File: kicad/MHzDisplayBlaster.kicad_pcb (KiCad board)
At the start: 2 copper layers, 50 x 39 mm, 7 parts, among them J1 Conn_02x15 DigitLHS, J2 Conn_02x15 DigitRHS, J3 Conn_01x03_Pin, U1 DC56-11GWA, U2 74LS04

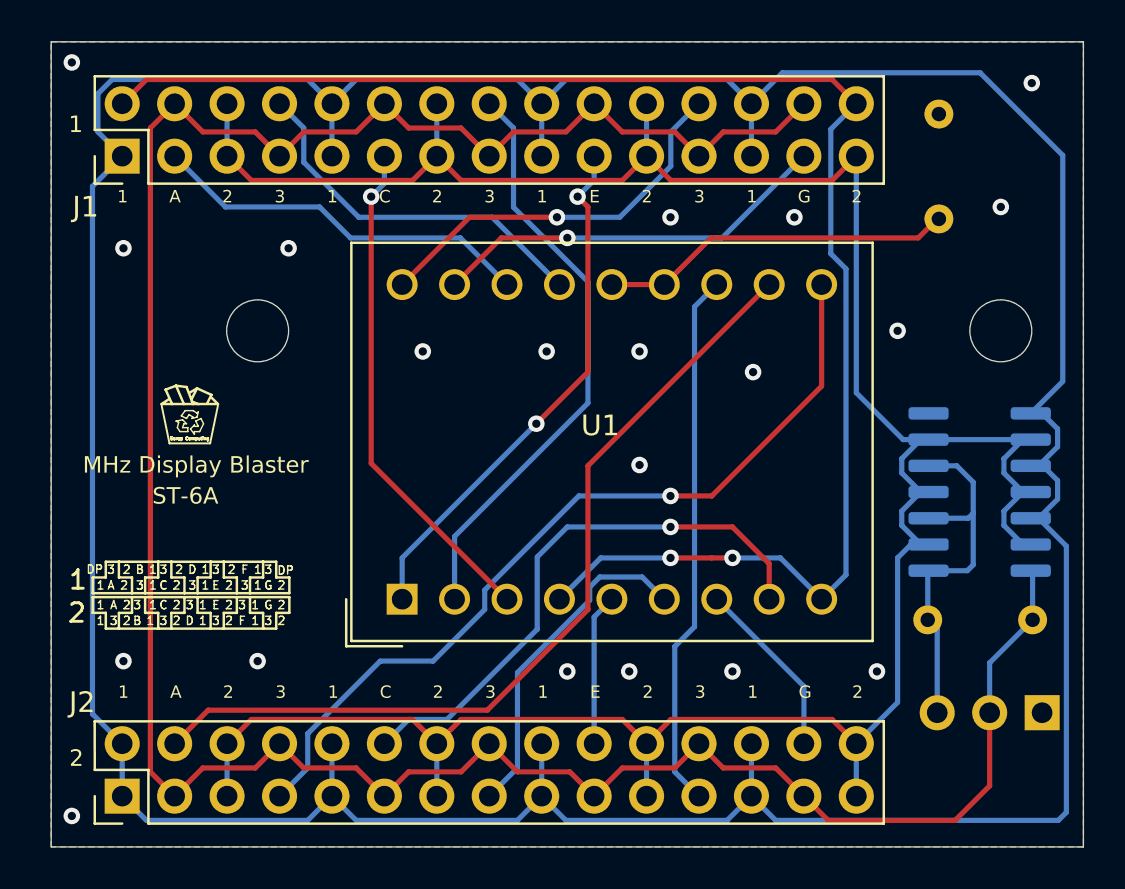
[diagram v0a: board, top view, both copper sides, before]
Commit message: Add Turbo LED Header
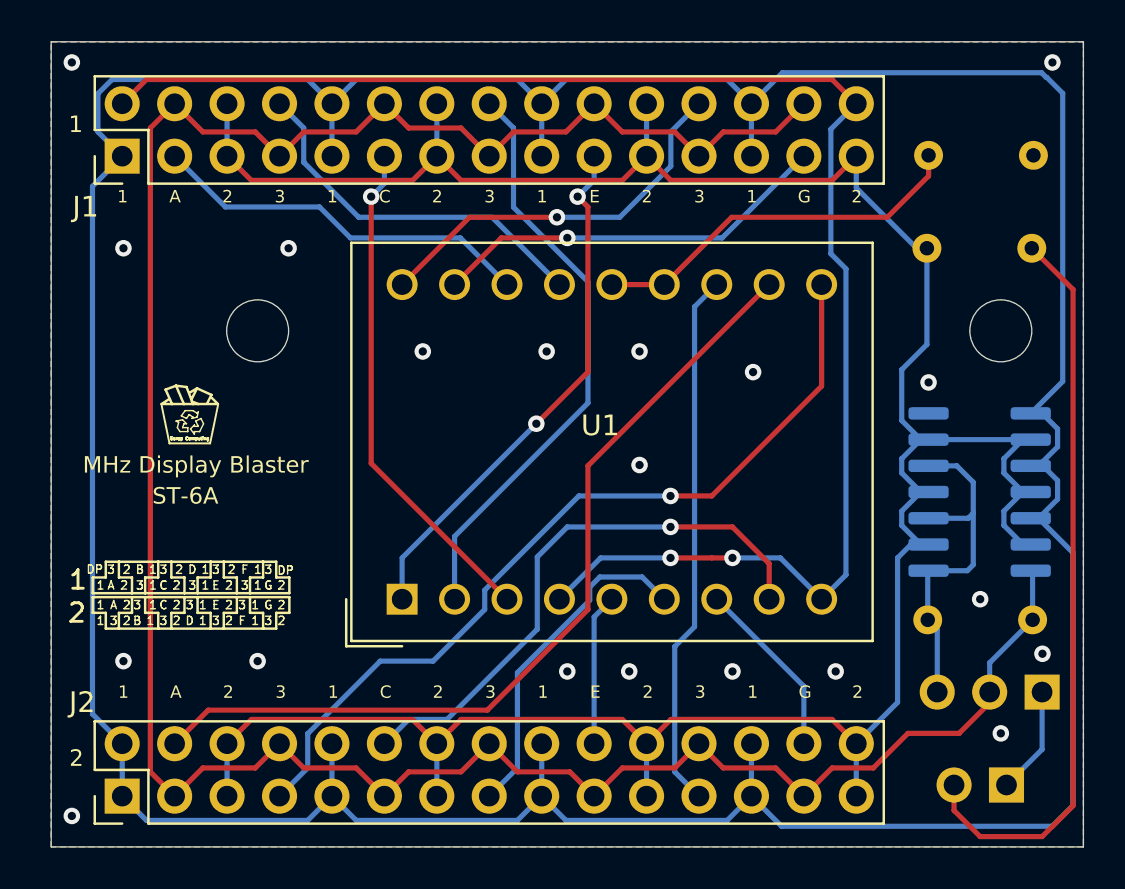
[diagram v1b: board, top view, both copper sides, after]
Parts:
- added J4: Conn_01x02_Pin, Connector_PinHeader_2.54mm:PinHeader_1x02_P2.54mm_Vertical, B.Cu at (146.3, 76.0)
- added R3: 1K, Resistor_THT:R_Axial_DIN0204_L3.6mm_D1.6mm_P5.08mm_Horizontal, B.Cu at (147.5, 50.0)
- moved R1 5.00 mm to (147.6, 45.5), turned to 180 degrees
- moved J3 1.00 mm to (148.0, 71.5)
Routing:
- net Net-(J4-Pin_2): track 0.00 -> 36.0 mm
- net GND: track 0.00 -> 5.71 mm
- net 3: track 129.6 -> 126.3 mm
- net 1: track 188.3 -> 190.5 mm
- net DIG1_CC: track 17.3 -> 18.5 mm
- net Turbo: track 18.1 -> 17.1 mm
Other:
- board text removed: "+5"
- board text removed: "Gnd"
- board text removed: "Trbo"

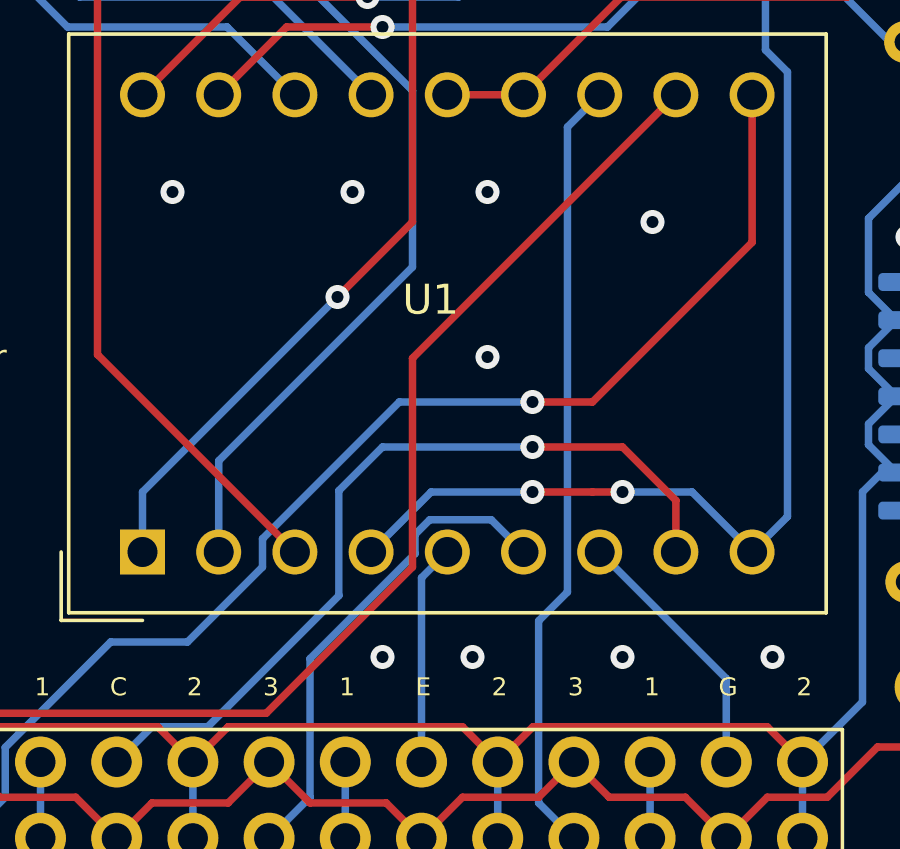
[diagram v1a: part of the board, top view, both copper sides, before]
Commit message: Adjust ground plane vias
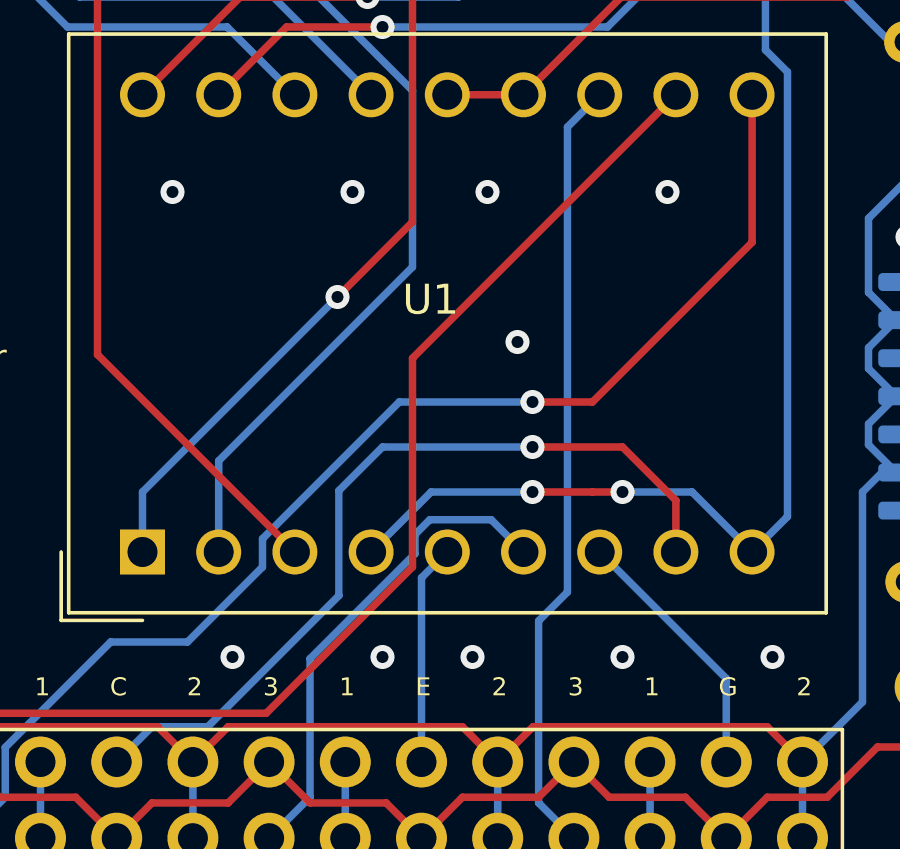
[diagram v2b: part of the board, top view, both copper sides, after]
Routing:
- net GND: vias 20 -> 21
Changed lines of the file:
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@@
   (via (at 133 70.5) (size 0.8) (drill 0.4) (layers "F.Cu" "B.Cu") (free) (net 21))
   (via (at 142.5 56.5) (size 0.8) (drill 0.4) (layers "F.Cu" "B.Cu") (free) (net 21))
-  (via (at 128.5 60.5) (size 0.8) (drill 0.4) (layers "F.Cu" "B.Cu") (free) (net 21))
+  (via (at 129.5 60) (size 0.8) (drill 0.4) (layers "F.Cu" "B.Cu") (free) (net 21))
   (via (at 103.5 70) (size 0.8) (drill 0.4) (layers "F.Cu" "B.Cu") (free) (net 21))
   (via (at 148.016689 69.644067) (size 0.8) (drill 0.4) (layers "F.Cu" "B.Cu") (free) (net 21))
@@
   (via (at 101 41) (size 0.8) (drill 0.4) (layers "F.Cu" "B.Cu") (free) (net 21))
   (via (at 110 70) (size 0.8) (drill 0.4) (layers "F.Cu" "B.Cu") (free) (net 21))
-  (via (at 134 56) (size 0.8) (drill 0.4) (layers "F.Cu" "B.Cu") (free) (net 21))
+  (via (at 134.5 55) (size 0.8) (drill 0.4) (layers "F.Cu" "B.Cu") (free) (net 21))
   (via (at 138 70.5) (size 0.8) (drill 0.4) (layers "F.Cu" "B.Cu") (free) (net 21))
   (via (at 125 70.5) (size 0.8) (drill 0.4) (layers "F.Cu" "B.Cu") (free) (net 21))
@@
   (via (at 128.5 55) (size 0.8) (drill 0.4) (layers "F.Cu" "B.Cu") (free) (net 21))
   (via (at 124 55) (size 0.8) (drill 0.4) (layers "F.Cu" "B.Cu") (free) (net 21))
+  (via (at 120 70.5) (size 0.8) (drill 0.4) (layers "F.Cu" "B.Cu") (free) (net 21))
   (via (at 148.5 41) (size 0.8) (drill 0.4) (layers "F.Cu" "B.Cu") (free) (net 21))
   (via (at 111.5 50) (size 0.8) (drill 0.4) (layers "F.Cu" "B.Cu") (free) (net 21))

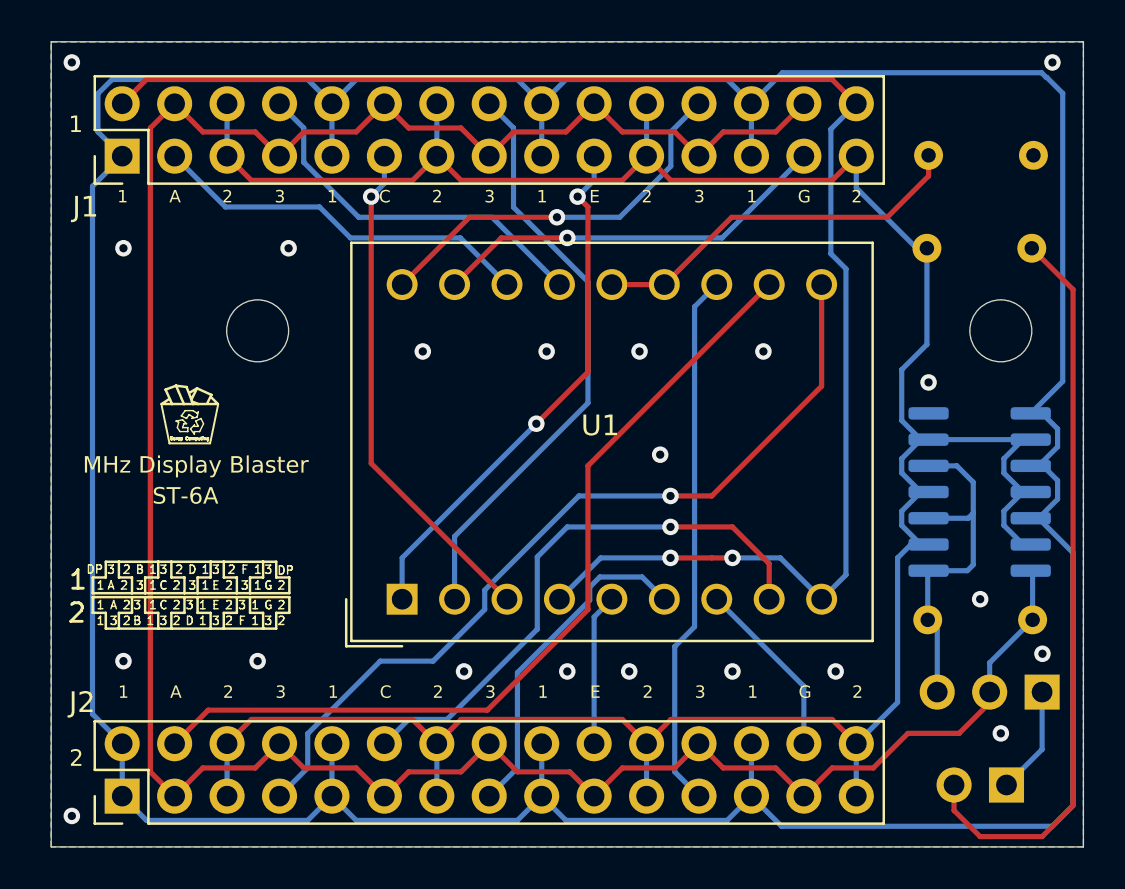
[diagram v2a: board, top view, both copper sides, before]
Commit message: Slight adjustment to display and mounting holes
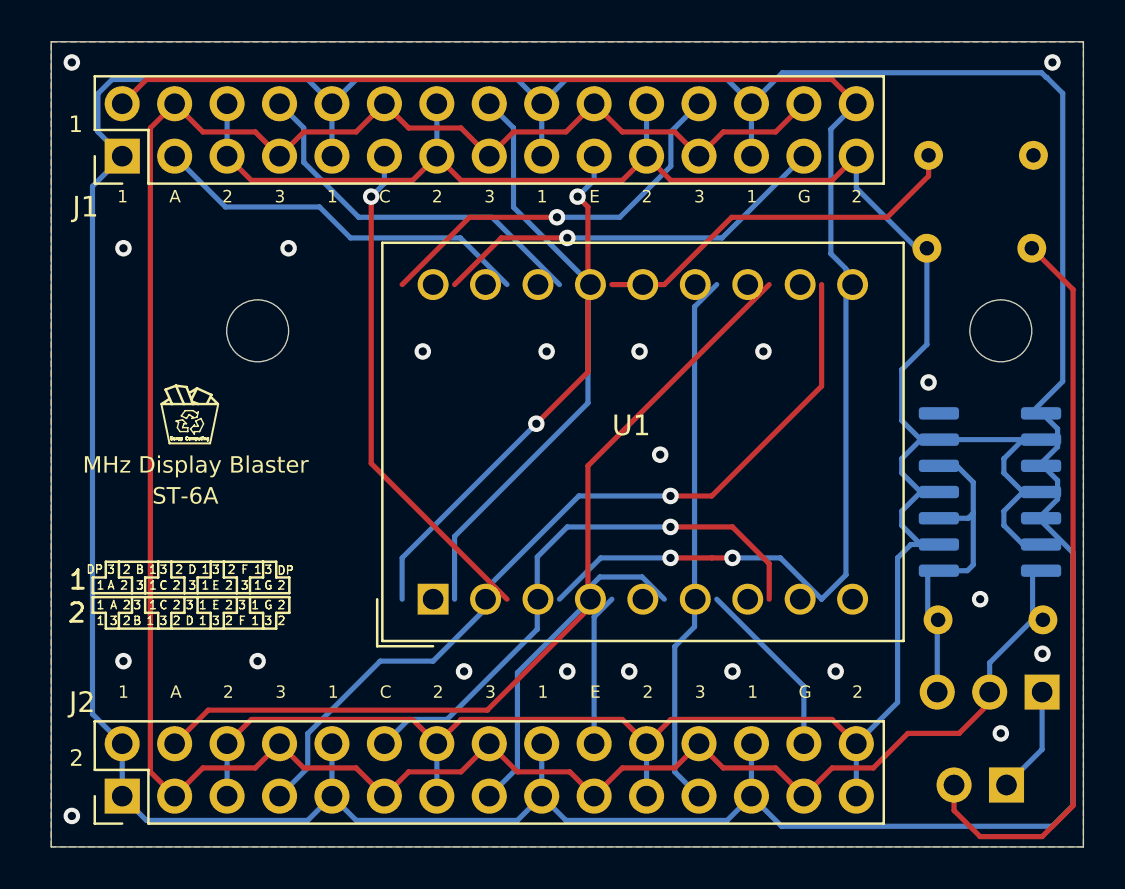
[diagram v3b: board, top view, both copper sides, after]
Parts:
- moved U1 1.50 mm to (118.5, 67.0)
- moved R2 0.50 mm to (148.0, 68.0)
- moved U2 0.50 mm to (145.5, 61.8)
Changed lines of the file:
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@@
   )
   (footprint "Display_7Segment:DA56-11CGKWA" locked (layer "F.Cu")
-    (at 117 67 90)
+    (at 118.5 67 90)
     (descr "http://www.kingbright.com/attachments/file/psearch/000/00/00/DA56-11CGKWA(Ver.16A).pdf")
     (tags "Double digit seven segment green LED display")
@@
   )
   (footprint "Resistor_THT:R_Axial_DIN0204_L3.6mm_D1.6mm_P5.08mm_Horizontal" (layer "B.Cu")
-    (at 147.54 68 180)
+    (at 148.04 68 180)
     (descr "Resistor, Axial_DIN0204 series, Axial, Horizontal, pin pitch=5.08mm, 0.167W, length*diameter=3.6*1.6mm^2, http://cdn-reichelt.de/documents/datenblatt/B400/1_4W%23YAG.pdf")
     (tags "Resistor Axial_DIN0204 series Axial Horizontal pin pitch 5.08mm 0.167W length 3.6mm diameter 1.6mm")
@@
   )
   (footprint "Package_SO:SOIC-14_3.9x8.7mm_P1.27mm" (layer "B.Cu")
-    (at 144.975 61.81)
+    (at 145.475 61.81)
     (descr "SOIC, 14 Pin (JEDEC MS-012AB, https://www.analog.com/media/en/package-pcb-resources/package/pkg_pdf/soic_narrow-r/r_14.pdf), generated with kicad-footprint-generator ipc_gullwing_generator.py")
     (tags "SOIC SO")

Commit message: Change HEX Inverter position, clean up layout
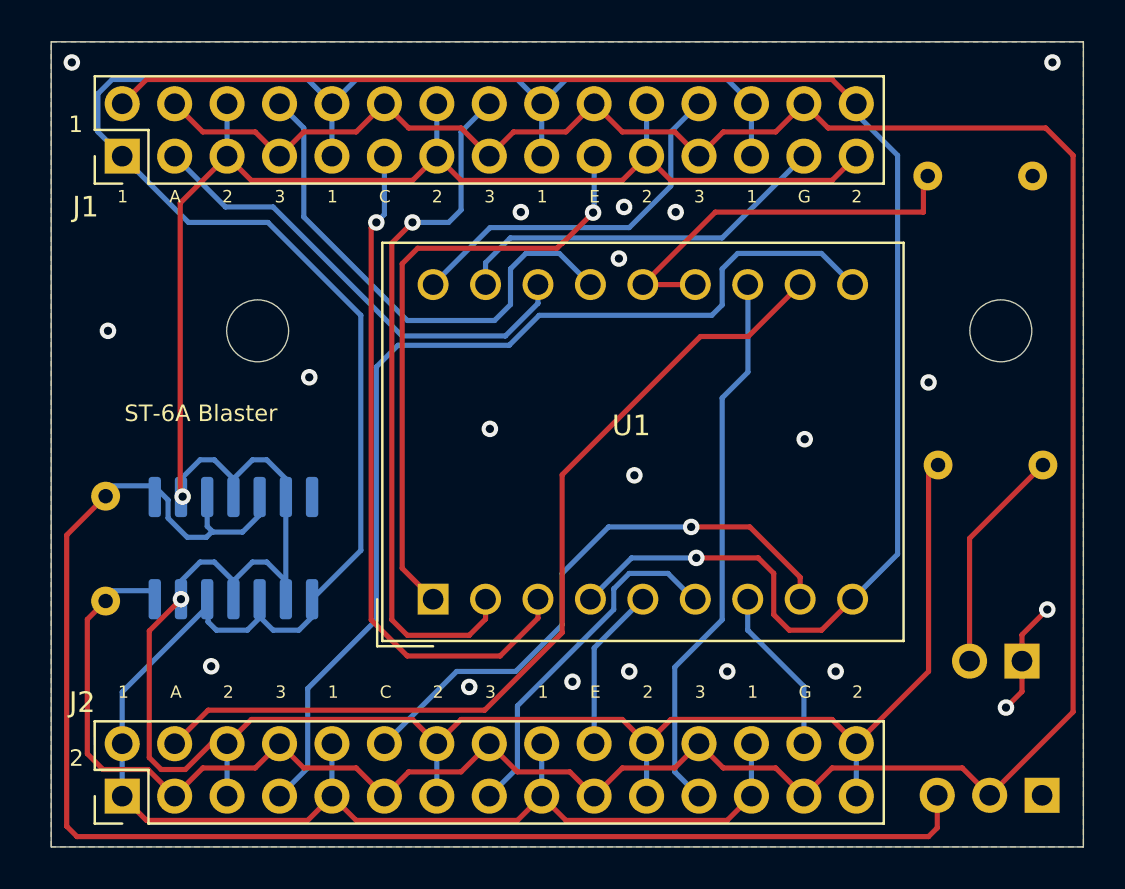
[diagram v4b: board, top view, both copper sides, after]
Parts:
- R3: value 1K -> 330
- moved R2 45.4 mm to (102.6, 67.1), turned to 90 degrees
- moved U2 36.7 mm to (108.8, 64.5), turned to -90 degrees
- moved R3 10.5 mm to (148.0, 60.5)
- moved J4 6.05 mm to (147.0, 70.0)
- moved J3 5.00 mm to (148.0, 76.5)
- moved R1 1.00 mm to (147.5, 46.5)
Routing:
- net Turbo: track 17.1 -> 74.6 mm
- net 1: track 190.5 -> 137.4 mm
- net Net-(J4-Pin_2): track 36.0 -> 11.0 mm
- net 3: track 126.3 -> 145.6 mm
- net 2: track 132.9 -> 150.1 mm, vias 0 -> 2
- net DIG2_B: track 40.9 -> 49.7 mm, vias 1 -> 0
- net DIG1_C: track 24.5 -> 33.2 mm
- net DIG1_B: track 18.2 -> 24.9 mm
- net DIG1_D: track 28.7 -> 34.1 mm, vias 0 -> 1
- net DIG1_E: track 25.7 -> 29.9 mm, vias 2 -> 1
- net DIG1_A: track 18.7 -> 22.8 mm
- net DP: track 76.2 -> 79.0 mm, vias 2 -> 1
- net DIG2_A: track 42.1 -> 44.0 mm
- net DIG1_F: track 19.0 -> 18.0 mm, vias 1 -> 0
- net DIG2_D: track 16.4 -> 17.3 mm
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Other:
- board text added: "330"
- board text added: "5v"
- board text added: "Gnd"
- board text added: "LED+"
- board text added: "LED-"
- board text added: "ST-6A Blaster"
- board text added: "Trbo"
- board text removed: "MHz Display Blaster"
- board text removed: "ST-6A"

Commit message: Rotate HEX inverter, finalize
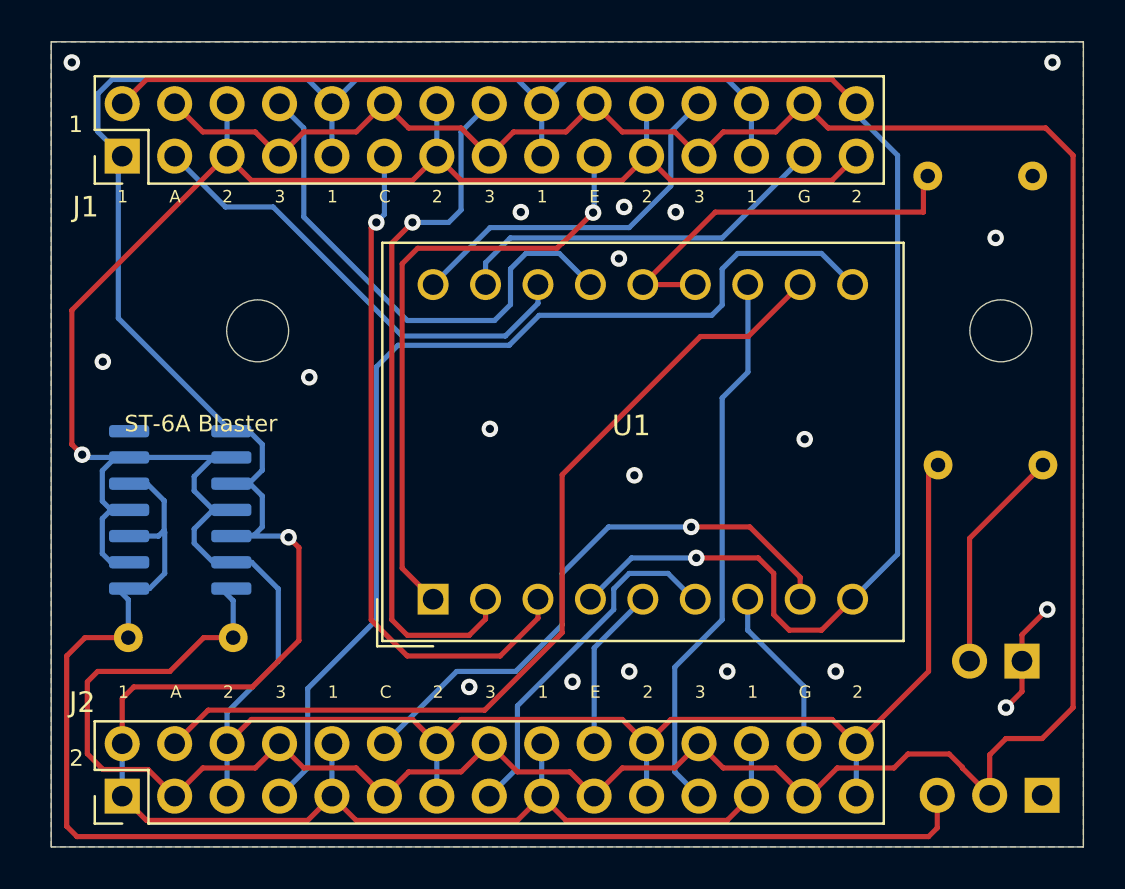
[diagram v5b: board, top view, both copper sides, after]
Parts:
- moved R2 6.43 mm to (108.8, 68.9), turned to 180 degrees
- moved U2 3.17 mm to (106.2, 62.7), turned to 0 degrees
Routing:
- net 3: track 145.6 -> 151.1 mm
- net Turbo: track 74.6 -> 69.2 mm
- net 1: track 137.4 -> 134.7 mm, vias 0 -> 1
- net 2: track 150.1 -> 150.5 mm, vias 2 -> 1
- net GND: vias 20 -> 19
